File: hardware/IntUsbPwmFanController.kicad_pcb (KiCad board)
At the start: 2 copper layers, 35 x 75 mm, 57 parts, among them J3 PC power, J6 FAN, J7 USB_Out, J8 GPIO, Q1 IRLML6402, U1 FT260S, U2 AT24CS01-SSHM, U3 ATtiny202-SS

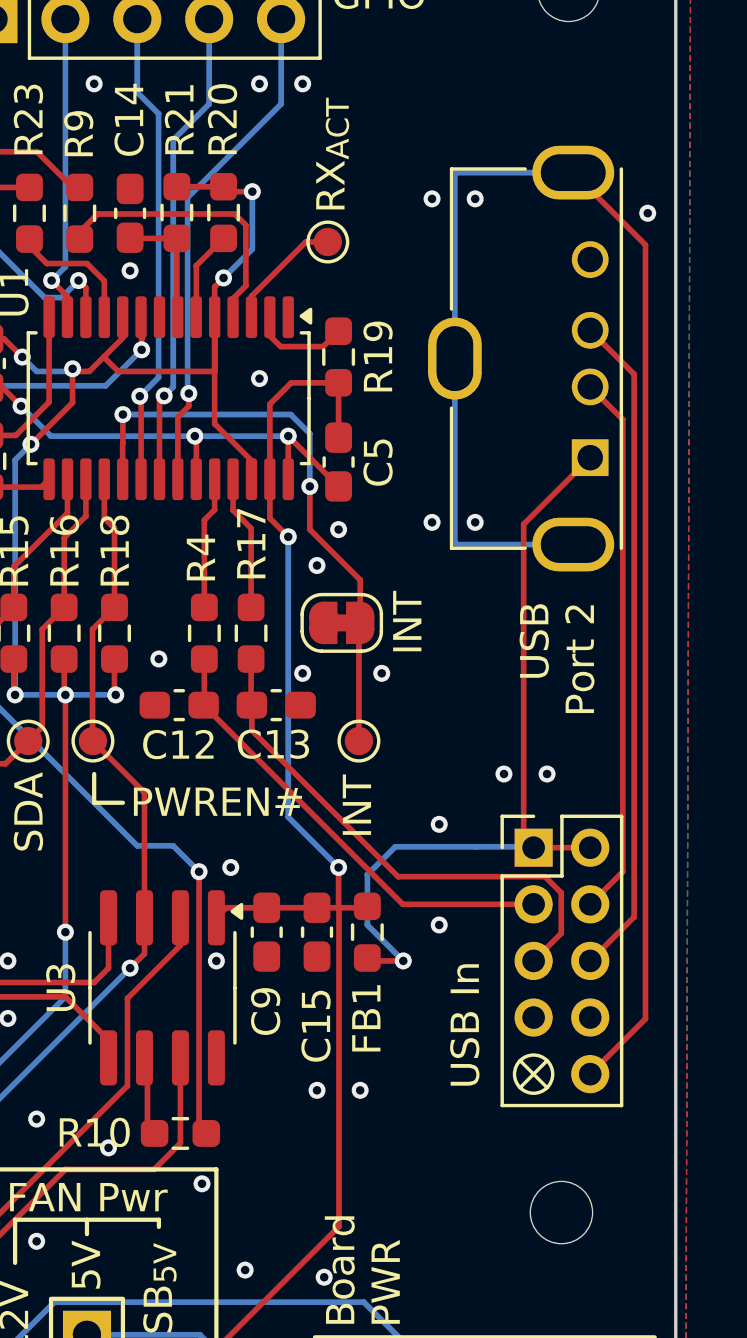
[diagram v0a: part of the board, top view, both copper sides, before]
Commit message: Adjust schematic and PCB to the new footprint
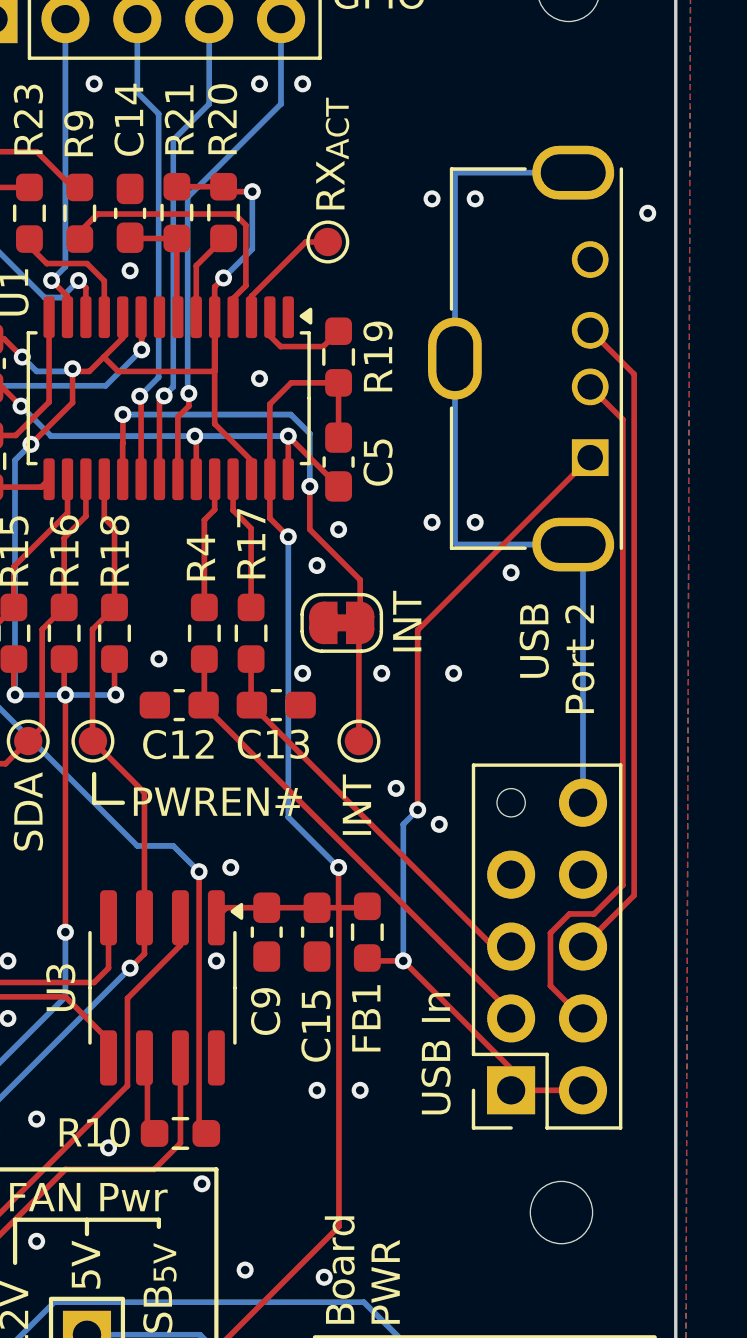
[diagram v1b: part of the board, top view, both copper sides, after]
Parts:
- J1: footprint USB:Internal USB 2.0 Pinheader -> USB:Internal USB 2.0 Socket Default
- moved J1 8.61 mm to (179.3, 59.7), turned to 180 degrees
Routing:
- net S-GND: track 55.2 -> 30.7 mm
- net USB2-: track 19.2 -> 24.8 mm
- net USB1+: track 18.6 -> 14.3 mm
- net VUSB: track 28.2 -> 30.7 mm, vias 1 -> 2
- net USB1-: track 16.2 -> 17.2 mm

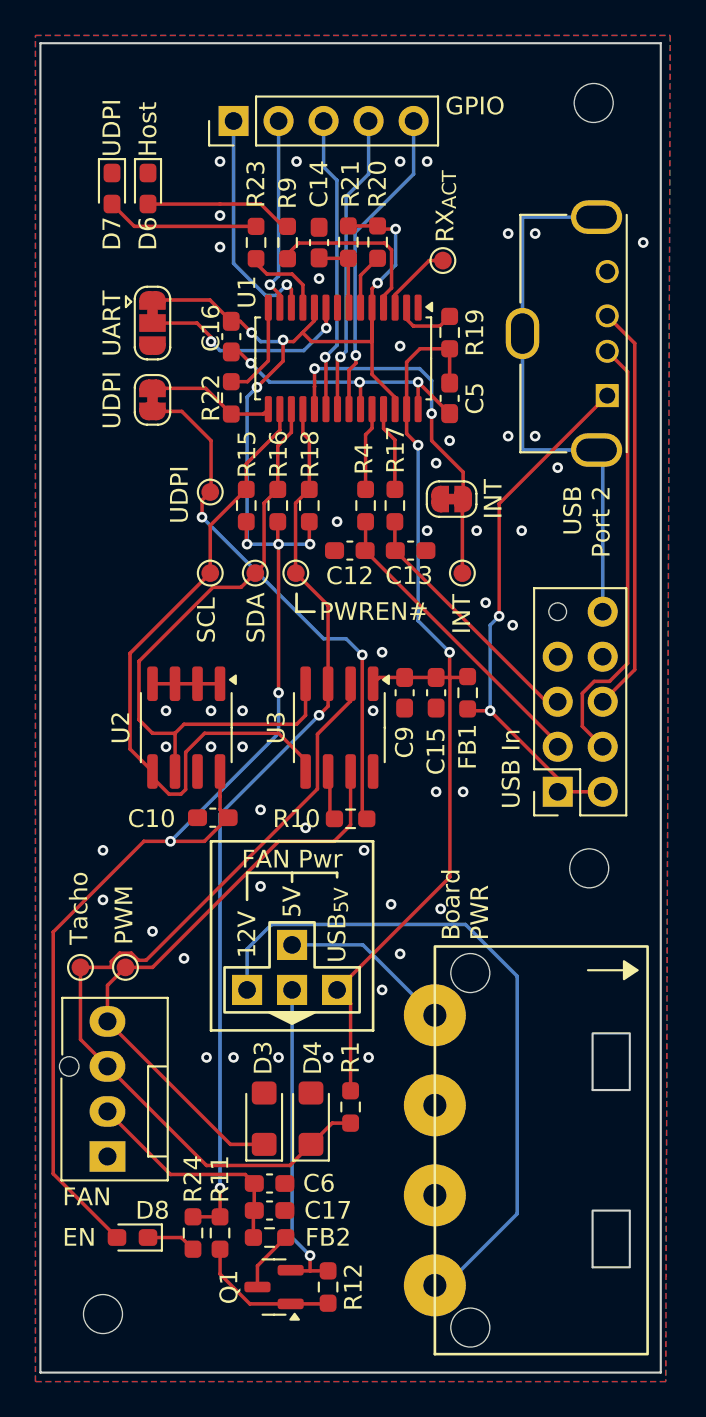
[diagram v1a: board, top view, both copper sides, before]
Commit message: Switch to a pinheader for the USB connector
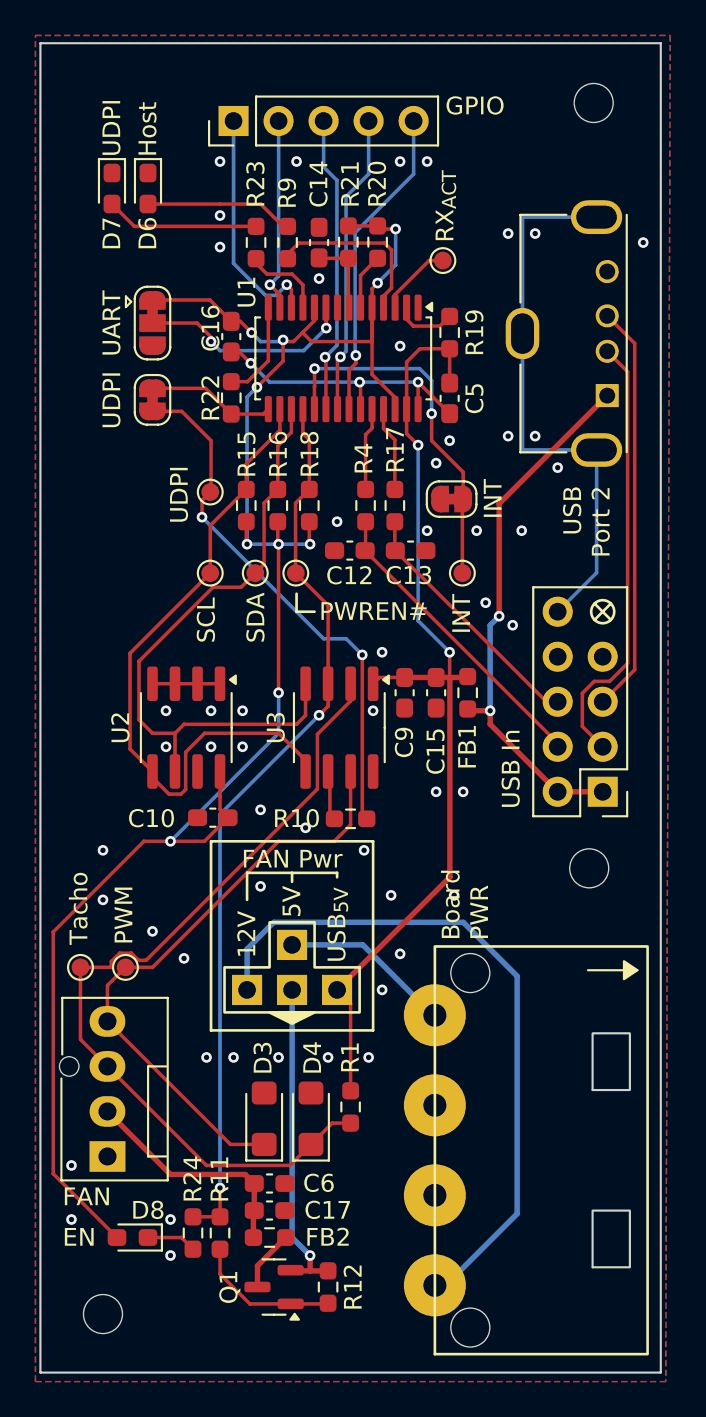
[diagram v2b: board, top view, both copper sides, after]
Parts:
- J1: footprint USB:Internal USB 2.0 Socket Default -> USB:Internal USB 2.0 Header Default
- moved J1 2.54 mm to (181.9, 59.7)
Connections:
- J1 pad 2: USB1- -> USB2-
- J1 pad 3: USB2- -> USB1-
- J1 pad 4: USB1+ -> USB2+
- J1 pad 5: USB2+ -> USB1+
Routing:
- net S-GND: track 30.7 -> 32.0 mm
- net GND: vias 52 -> 56

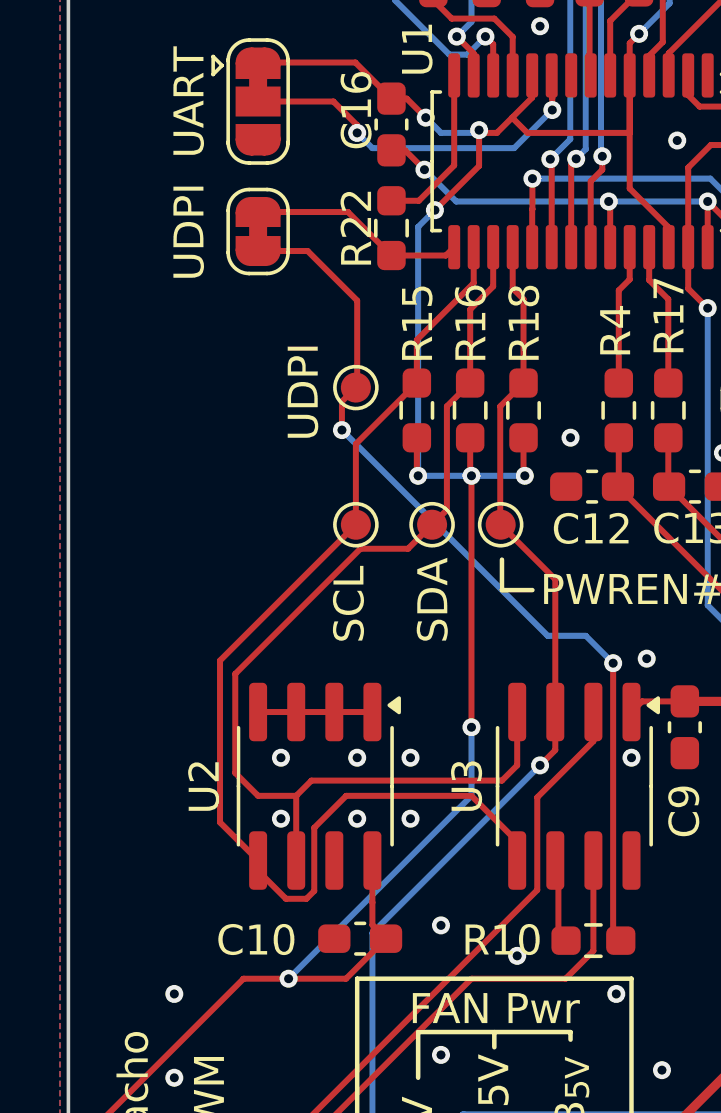
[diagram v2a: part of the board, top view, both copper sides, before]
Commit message: Add Labels and CC to PCB
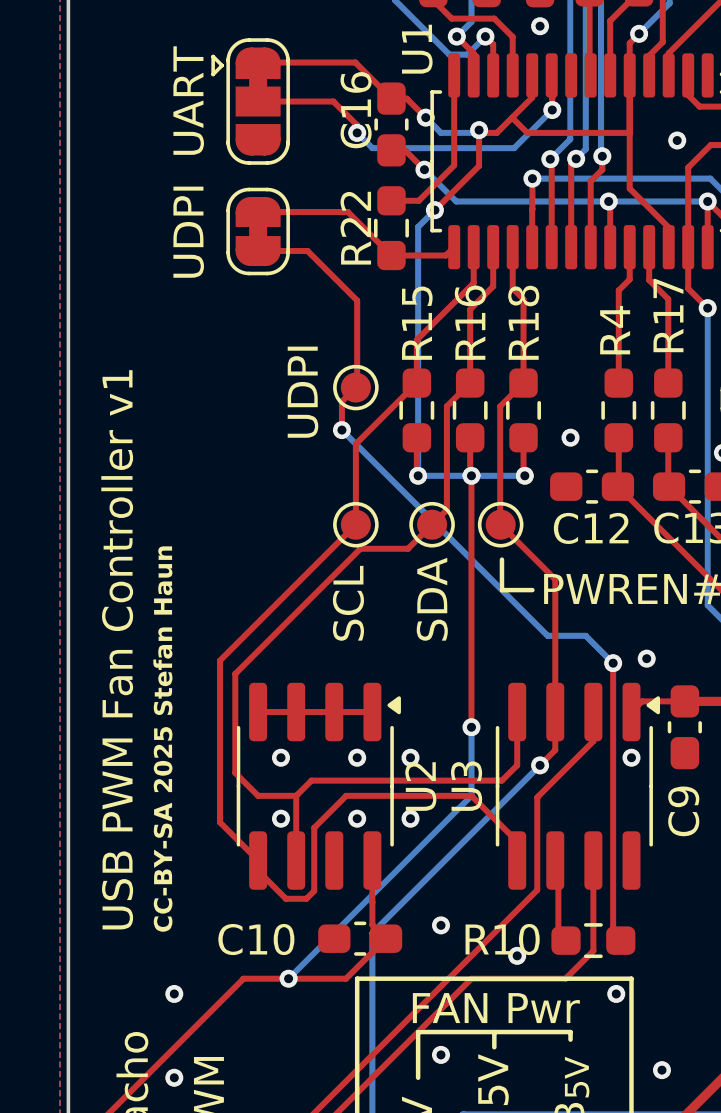
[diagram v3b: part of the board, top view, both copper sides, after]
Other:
- board text added: "CC-BY-SA 2025 Stefan Haun"
- board text added: "USB PWM Fan Controller v1"
- board text added: "https://github.com/penguineer/IntUsbPwmFanController"
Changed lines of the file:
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@@
 		(tags "SOIC SO")
 		(property "Reference" "U2"
-			(at 0 3.683 90)
+			(at 0 -3.556 90)
 			(layer "F.SilkS")
 			(effects
@@
 		)
 	)
+	(gr_text "USB PWM Fan Controller v1"
+		(at 152.4 60.96 90)
+		(layer "F.SilkS")
+		(effects
+			(font
+				(size 1 1)
+				(thickness 0.15)
+			)
+			(justify left bottom)
+		)
+	)
 	(gr_text "UDPI"
 		(at 157.988 42.926 90)
@@
 		)
 	)
+	(gr_text "CC-BY-SA 2025 Stefan Haun"
+		(at 153.67 60.96 90)
+		(layer "F.SilkS")
+		(effects
+			(font
+				(size 0.6 0.6)
+				(thickness 0.1)
+				(bold yes)
+			)
+			(justify left bottom)
+		)
+	)
 	(gr_text "USB In"
 		(at 177.292 56.134 90)
@@
 		)
 	)
+	(gr_text "https://github.com/penguineer/IntUsbPwmFanController"
+		(at 152.4 19.05 90)
+		(layer "B.SilkS")
+		(effects
+			(font
+				(size 1 1)
+				(thickness 0.15)
+			)
+			(justify left bottom mirror)
+		)
+	)
